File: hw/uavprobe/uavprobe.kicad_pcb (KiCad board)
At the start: 2 copper layers, 31 x 120.2 mm, 124 parts, among them IC1 UCLAMP3306P.TCT, J1 USB_C_Receptacle_USB2.0_14P, J10 SERIAL1 (flow), J11 SERIAL1 (GPS/I2C), J12 SERIAL1 (Lidar), J13 I^{2}C (Lidar), J14 I^{2}C, J15 USB2, J16 CAN1, J17 CAN2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

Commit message: Back silkscreen
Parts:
- added REF**: OSHW-Logo2_14.6x12mm_SilkScreen, Symbol:OSHW-Logo2_14.6x12mm_SilkScreen, B.Cu at (116.5, 37.0)
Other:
- board text added: "UAV sensor probe https://github.com/Ecognize/uavprobe Rev.: ${REVISION} Date: ${ISSUE_DATE}"

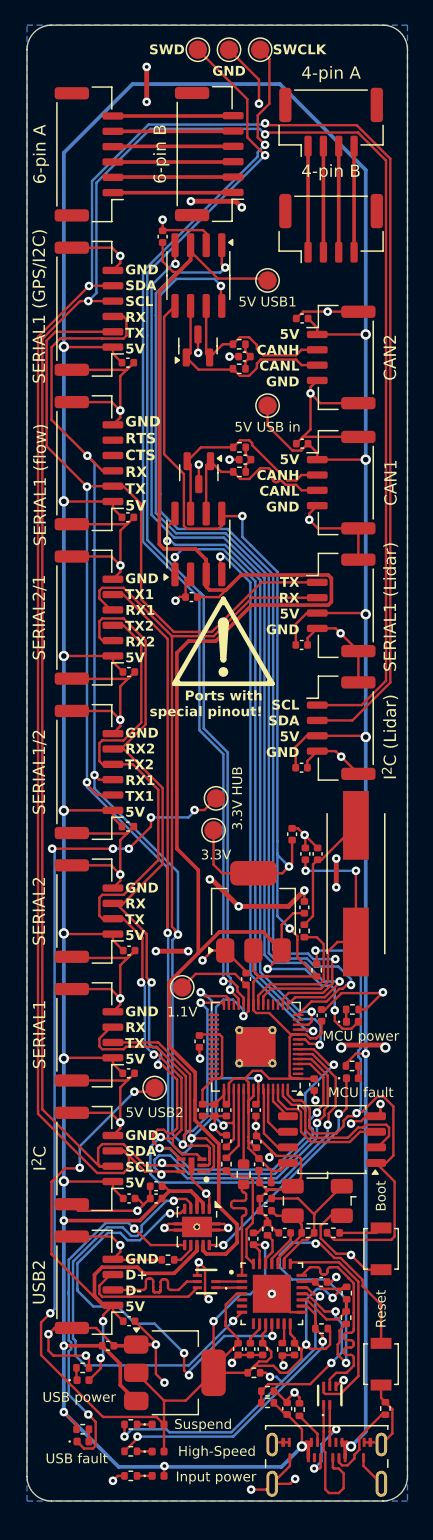
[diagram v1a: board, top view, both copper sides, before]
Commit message: USB-C connector change
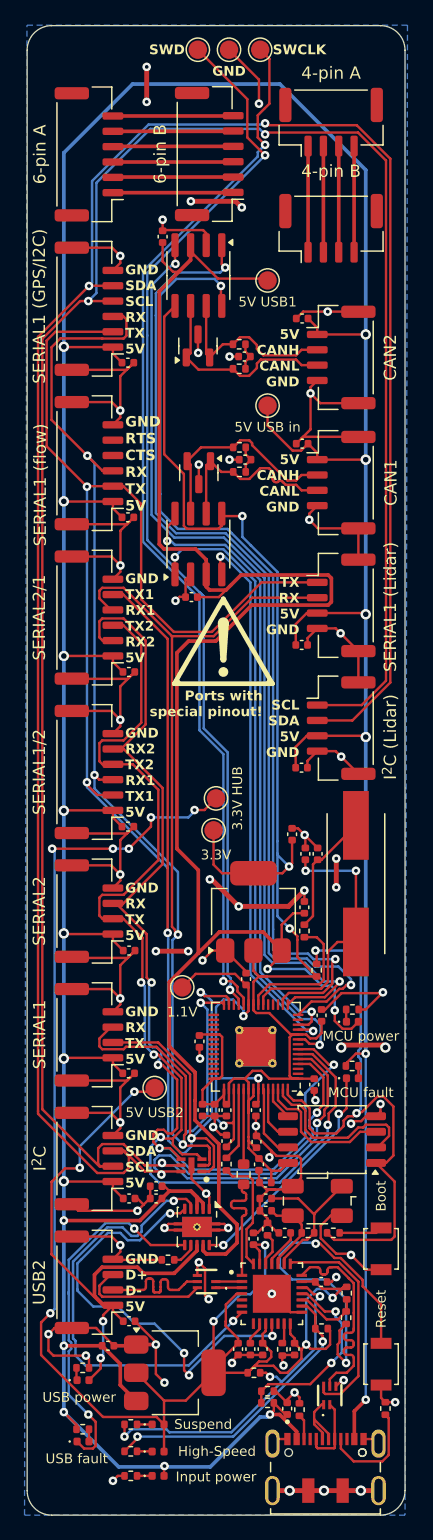
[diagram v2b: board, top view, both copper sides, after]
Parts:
- J1: footprint Connector_USB:USB_C_Receptacle_Amphenol_124019772112A -> Import:JAE_DX07S016JA1R1500
- moved J1 2.37 mm to (131.9, 141.8)
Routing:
- net /USB/USBC_D+: track 11.8 -> 5.58 mm
- net /Connectors/VBUS: track 368.8 -> 363.6 mm
- net GND: track 323.1 -> 318.9 mm, vias 63 -> 65
- net /USB/USBC_D-: track 8.95 -> 5.87 mm, vias 2 -> 0
- net Net-(J1-CC2): track 6.75 -> 8.71 mm
- net Net-(J1-CC1): track 2.77 -> 2.04 mm
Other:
- board size 31 x 120.2 mm -> 30.8 x 121.4 mm

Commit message: LEDs reconfigured for 10 mA current
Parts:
- R20, R21, R27: value 150R -> 320R
- R22, R24: value 10R -> 150R
- R26, R28: value 95R -> 210R
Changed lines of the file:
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@@
 			)
 		)
-		(property "Value" "95R"
+		(property "Value" "210R"
 			(at 0 1.17 0)
 			(layer "F.Fab")
@@
 			)
 		)
-		(property "Value" "10R"
+		(property "Value" "150R"
 			(at 0 1.17 0)
 			(layer "F.Fab")
@@
 			)
 		)
-		(property "Value" "10R"
+		(property "Value" "150R"
 			(at 0 1.17 0)
 			(layer "F.Fab")
@@
 			)
 		)
-		(property "Value" "95R"
+		(property "Value" "210R"
 			(at 0 1.17 0)
 			(layer "F.Fab")
@@
 			)
 		)
-		(property "Value" "150R"
+		(property "Value" "320R"
 			(at 0 1.17 0)
 			(layer "F.Fab")
@@
 			)
 		)
-		(property "Value" "150R"
+		(property "Value" "320R"
 			(at 0 1.17 0)
 			(layer "F.Fab")
@@
 			)
 		)
-		(property "Value" "150R"
+		(property "Value" "320R"
 			(at 0 1.17 0)
 			(layer "F.Fab")
